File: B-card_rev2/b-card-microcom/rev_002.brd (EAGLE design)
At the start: 88.9 x 50.8 mm, 55 parts, among them IC1 AZ1117IH-5.0, IC2 AZ1117IH-5.0, IC3 AZ1117IH-5.0, IC4 DMN2041L-7, IC5 DMN2041L-7, IC6 DMN2041L-7, IC7 AZ1117IH-3.3, J1 10118192-0002LF, SW1 B3AL-1000P, U1 ATMEGA32U4-MU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

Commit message: Inverted QR
QR looks like poo, I may thin it out.
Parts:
- removed U$1: (no value), b-card-link:LINK
- added U$3: (no value), b-card-link:LINK_INV
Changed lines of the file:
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@@
 <layer number="98" name="Guide" color="6" fill="1" visible="no" active="no"/>
 <layer number="99" name="SpiceOrder" color="5" fill="1" visible="no" active="no"/>
+<layer number="200" name="200bmp" color="1" fill="10" visible="yes" active="yes"/>
 </layers>
 <board>
@@
 <attribute name="SPICEPREFIX" value="C" x="60.96" y="37.465" size="1.778" layer="27" rot="R180" display="off"/>
 </element>
-<element name="U$1" library="b-card-link" package="LINK" value="" x="54.2925" y="4.1275" smashed="yes"/>
 <element name="U$2" library="b-card-link" package="MCOM" value="" x="38.735" y="4.1275" smashed="yes"/>
+<element name="U$3" library="b-card-link" package="LINK_INV" value="" x="53.975" y="3.81" smashed="yes"/>
 </elements>
 <signals>
@@
 </signals>
 <mfgpreviewcolors>
-<mfgpreviewcolor name="soldermaskcolor" color="0xC8008000"/>
+<mfgpreviewcolor name="soldermaskcolor" color="0xC8000000"/>
 <mfgpreviewcolor name="silkscreencolor" color="0xFFFEFEFE"/>
-<mfgpreviewcolor name="backgroundcolor" color="0xFF282828"/>
-<mfgpreviewcolor name="coppercolor" color="0xFFFFBF00"/>
-<mfgpreviewcolor name="substratecolor" color="0xFF786E46"/>
+<mfgpreviewcolor name="backgroundcolor" color="0xFFCACACA"/>
+<mfgpreviewcolor name="coppercolor" color="0xFFC6C6C6"/>
+<mfgpreviewcolor name="substratecolor" color="0xFF14120B"/>
 </mfgpreviewcolors>
 </board>

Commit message: update
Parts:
- removed U$3: (no value), b-card-link:LINK_INV
- added U$1: (no value), b-card-link:LINK_INV
- moved R5 2.01 mm to (80.0, 35.6)
- moved R6 1.42 mm to (80.0, 38.1)
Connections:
- net USBA_N: now also R5.1; no longer R6.1
- net USBA_P: now also R6.1; no longer R5.1
- net USBB_N: now also J1.2, R5.2; no longer J1.3, R6.2
- net USBB_P: now also J1.3, R6.2; no longer J1.2, R5.2
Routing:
- net USBA_P: track 8.83 -> 11.4 mm
- net USBB_P: track 6.80 -> 4.90 mm
- net USBA_N: track 12.4 -> 11.4 mm
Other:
- board text added: "SCAN ME"

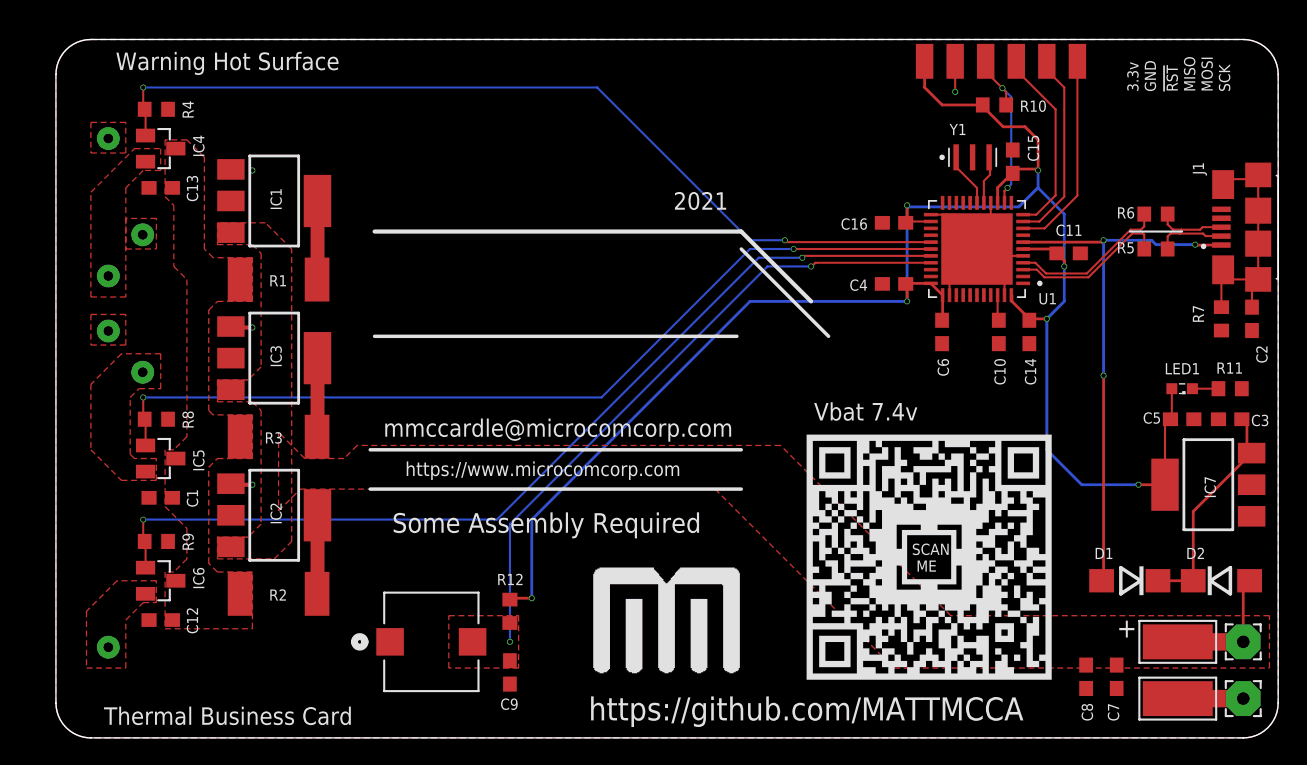
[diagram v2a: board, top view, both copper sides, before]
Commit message: not rev-ed
Changed the sch and board, adapted for higher current.
Made small change to sketch, removed thermal approx.
exported new Gerber's.
changed BOM to reflect new design.

layout change now ready for fab, still needs a once over to correct any mistakes that I may have missed.
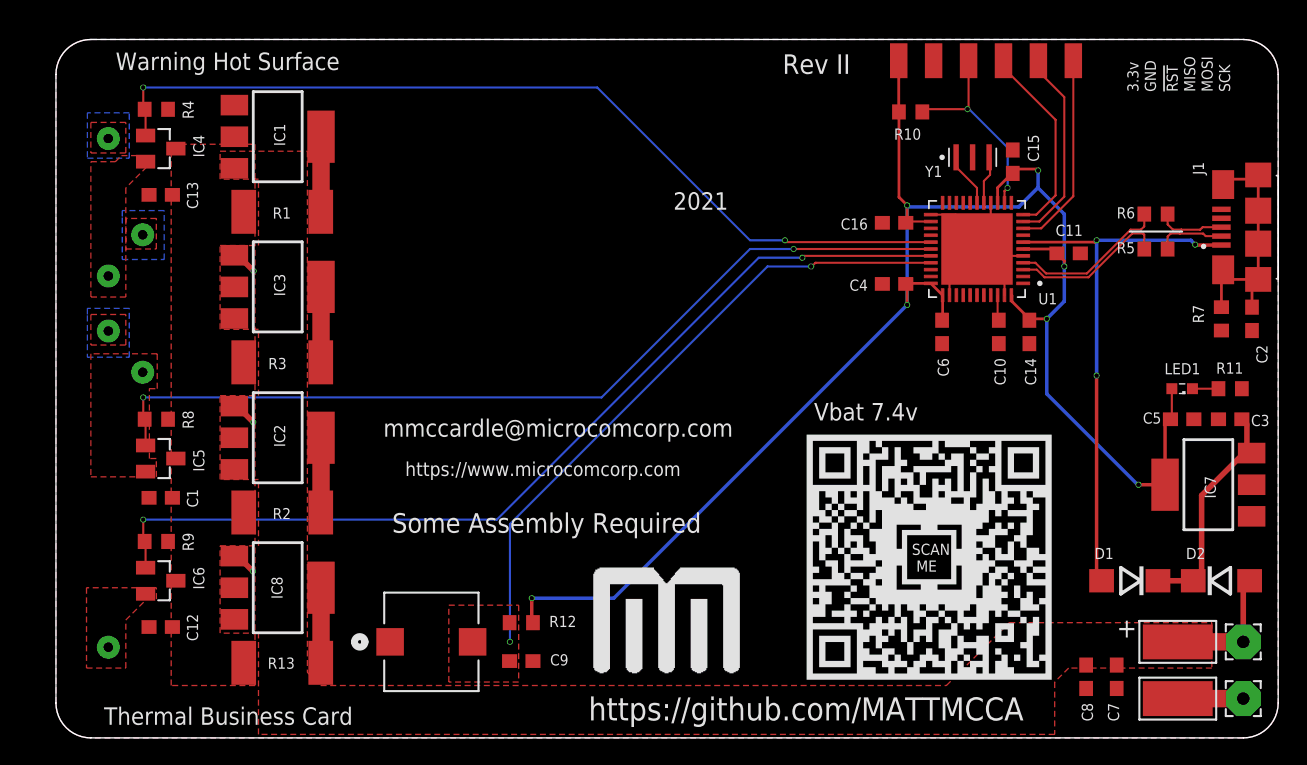
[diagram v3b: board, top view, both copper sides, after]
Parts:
- added IC8: AZ1117IH-5.0, v-reg-edit:SOT223
- added R13: 5.6, rcl:R2512
- R1, R2, R3: value 11 -> 5.6
- moved R10 6.12 mm to (62.2, 45.5)
- moved R2 5.92 mm to (16.5, 16.4)
- moved IC2 5.64 mm to (16.1, 21.8)
- moved R3 5.42 mm to (16.5, 27.3)
- moved IC3 5.19 mm to (16.1, 32.8)
- moved R1 4.93 mm to (16.5, 38.3)
- moved IC1 4.68 mm to (16.1, 43.7)
- moved PAD5 1.88 mm to (61.3, 49.3)
- moved PAD10 1.57 mm to (63.8, 49.3)
- moved PAD6 1.25 mm to (66.4, 49.3)
- moved C9 1.17 mm to (33.8, 5.59), turned to 0 degrees
- moved R12 1.17 mm to (33.8, 8.38), turned to 0 degrees
- moved PAD9 0.93 mm to (68.9, 49.3)
- moved PAD8 0.61 mm to (71.5, 49.3)
- moved C13 0.51 mm to (7.62, 39.5)
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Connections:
- new net N$1: IC8.2, IC8.4, R13.1
- net +5V: now also R13.2
- net +8V: now also IC8.3
- net GND: now also IC8.1
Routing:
- net +3V3: track 132.3 -> 124.0 mm
- net N$1: track 0.00 -> 5.47 mm
- net !RST: track 12.6 -> 15.1 mm
- net N$7: track 7.02 -> 5.49 mm
- net +4.1V: track 16.6 -> 17.1 mm
- net GND: vias 4 -> 3
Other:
- board text added: "Rev II"
